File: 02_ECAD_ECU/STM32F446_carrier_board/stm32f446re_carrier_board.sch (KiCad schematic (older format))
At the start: 1 part

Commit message: added submodules in the right place now
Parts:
- gave numbers to parts that had none: 1
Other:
- moved on the sheet: U1
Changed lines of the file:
@@
 $Descr A4 11693 8268
 encoding utf-8
-Sheet 1 1
+Sheet 1 2
 Title ""
 Date ""
@@
 $EndDescr
 $Comp
-L MCU_ST_STM32F4:STM32F446RETx U?
+L MCU_ST_STM32F4:STM32F446RETx U1
 U 1 1 6138BFE8
-P 4000 3800
-F 0 "U?" H 4000 1911 50  0000 C CNN
-F 1 "STM32F446RETx" H 4000 1820 50  0000 C CNN
-F 2 "Package_QFP:LQFP-64_10x10mm_P0.5mm" H 3400 2100 50  0001 R CNN
-F 3 "http://www.st.com/st-web-ui/static/active/en/resource/technical/document/datasheet/DM00141306.pdf" H 4000 3800 50  0001 C CNN
-	1    4000 3800
+P 6700 3750
+F 0 "U1" H 6700 1861 50  0000 C CNN
+F 1 "STM32F446RETx" H 6700 1770 50  0000 C CNN
+F 2 "Package_QFP:LQFP-64_10x10mm_P0.5mm" H 6100 2050 50  0001 R CNN
+F 3 "http://www.st.com/st-web-ui/static/active/en/resource/technical/document/datasheet/DM00141306.pdf" H 6700 3750 50  0001 C CNN
+	1    6700 3750
 	1    0    0    -1
 $EndComp
+$Sheet
+S 9300 3500 1600 1550
+U 614A3ED5
+F0 "connectors" 50
+F1 "connectors.sch" 50
+$EndSheet
 $EndSCHEMATC

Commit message: carrierboard stm32f446 finished v0.1
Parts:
- added C1, C4: 4.7u, Capacitor_SMD:C_1206_3216Metric, symbol Device:C_Small
- added C10, C12: 12p, Capacitor_SMD:C_0603_1608Metric, symbol Device:C_Small
- added C18, C19: 10p, Capacitor_SMD:C_0402_1005Metric, symbol Device:C_Small
- added C2, C3, C5, C6, C7, C?: 100n, Capacitor_SMD:C_0603_1608Metric, symbol Device:C_Small
- added C8: 1u, Capacitor_SMD:C_0805_2012Metric, symbol Device:C_Small
- added C9: 10n, Capacitor_SMD:C_0805_2012Metric, symbol Device:C_Small
- added D1: BLUE, LED_SMD:LED_0603_1608Metric, symbol Device:LED_Small
- added FB2: 600 @ 600MHz, Inductor_SMD:L_0805_2012Metric, symbol Device:Ferrite_Bead_Small
- added H1, H2, H3, H4: MountingHole_Pad, MountingHole:MountingHole_2.2mm_M2_Pad_Via, symbol Mechanical:MountingHole_Pad
- added R1, R4, R? (x2): 10k, Resistor_SMD:R_1206_3216Metric, symbol Device:R_Small
- added R2: 1.5k, Resistor_SMD:R_0805_2012Metric, symbol Device:R_Small
- added R3: 47, Resistor_SMD:R_0603_1608Metric, symbol Device:R_Small
- added R5, R6: 2.2k, Resistor_SMD:R_0805_2012Metric, symbol Device:R_Small
- added SW1: SW_SPDT, max_KiCAD_lib:SPDT_Slide_Switches, symbol Switch:SW_SPDT
- added U3: W25N01GVZEIG_TR, max_KiCAD_lib:SON127P800X600X80-9N, symbol max_KiCAD_lib:W25N01GVZEIG_TR
- added Y1: 16MHz, Crystal:Crystal_SMD_3225-4Pin_3.2x2.5mm, symbol Device:Crystal_GND24_Small
- added Y2: 32.768kHz, Crystal:Crystal_SMD_2012-2Pin_2.0x1.2mm, symbol Device:Crystal_Small
- U1: LCSC part # (none) -> -
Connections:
- net +3V3: now reaches U1.1 (VBAT)
- net +3V3: now also U1.19 (VDD), U1.32 (VDD), U1.48 (VDD), U1.64 (VDD), C1.1, C2.1, C3.1, C5.1, C6.1, C7.1, C?.1, FB2.2, R?.2, R?.2, SW1.1 (A), U3.8 (VCC)
- net PC2: now reaches U1.10 (PC2)
- net PC3: now reaches U1.11 (PC3)
- net GND: now reaches U1.12 (VSSA)
- net GND: now also U1.18 (VSS), U1.31 (VSS), U1.47 (VSS), U1.63 (VSS), C1.2, C10.2, C12.2, C18.2, C19.2, C2.2, C3.2, C4.2, C5.2, C6.2, C7.2, C8.2, C9.2, C?.2, H1.1, H2.1, H3.1, H4.1, R2.2, R4.2, R5.2, R6.2, SW1.3 (C), U3.4 (GND), Y1.2, Y1.4
- net +3.3VA: now reaches U1.13 (VDDA)
- net +3.3VA: now also C8.1, C9.1, FB2.1
- net PA0: now reaches U1.14 (PA0)
- net PA1: now reaches U1.15 (PA1)
- net LED_STATUS: now reaches U1.16 (PA2)
- net LED_STATUS: now also D1.2 (A)
- net PA3: now reaches U1.17 (PA3)
- net PC13: now reaches U1.2 (PC13)
- net PA4: now reaches U1.20 (PA4)
- net PA5: now reaches U1.21 (PA5)
- net PA6: now reaches U1.22 (PA6)
- net PA7: now reaches U1.23 (PA7)
- net PC4: now reaches U1.24 (PC4)
- net PC5: now reaches U1.25 (PC5)
- net PB0: now reaches U1.26 (PB0)
- net PB1: now reaches U1.27 (PB1)
- net at U1.28 (PB2): now also R4.1
- net PB10: now reaches U1.29 (PB10)
- net OSC32_IN: now reaches U1.3 (PC14)
- net OSC32_IN: now also C18.1, Y2.1
- net at U1.30 (VCAP_1): now also C4.1
- net SPI2_!CS: now reaches U1.33 (PB12)
- net SPI2_!CS: now also U3.1 (/CS)
- net SPI2_SCK: now reaches U1.34 (PB13)
- net SPI2_SCK: now also U3.6 (CLK)
- net SPI2_MISO: now reaches U1.35 (PB14)
- net SPI2_MISO: now also U3.2 (DO(IO1))
- net SPI2_MOSI: now reaches U1.36 (PB15)
- net SPI2_MOSI: now also U3.5 (DI(IO0))
- net FLASH_!HOLD: now reaches U1.37 (PC6)
- net FLASH_!HOLD: now also R?.1, U3.7 (/HOLD(IO3))
- net FLASH_!WP: now reaches U1.38 (PC7)
- net FLASH_!WP: now also R?.1, U3.3 (/WP(IO2))
- net PC8: now reaches U1.39 (PC8)
- net OSC32_OUT: now reaches U1.4 (PC15)
- net OSC32_OUT: now also C19.1, Y2.2
- net PC9: now reaches U1.40 (PC9)
- net PA8: now reaches U1.41 (PA8)
- net PA9: now reaches U1.42 (PA9)
- net PA10: now reaches U1.43 (PA10)
- net USB_D-: now reaches U1.44 (PA11)
- net USB_D+: now reaches U1.45 (PA12)
- net SWDIO: now reaches U1.46 (PA13)
- net SWCLK: now reaches U1.49 (PA14)
- net HSE_IN: now reaches U1.5 (PH0)
- net HSE_IN: now also C10.1, Y1.1
- net PA15: now reaches U1.50 (PA15)
- net PC10: now reaches U1.51 (PC10)
- net PC11: now reaches U1.52 (PC11)
- net PC12: now reaches U1.53 (PC12)
- net PD2: now reaches U1.54 (PD2)
- net SWO: now reaches U1.55 (PB3)
- net PB4: now reaches U1.56 (PB4)
- net PB5: now reaches U1.57 (PB5)
- net PB6: now reaches U1.58 (PB6)
- net PB7: now reaches U1.59 (PB7)
- net HSE_OUT: now reaches U1.6 (PH1)
- net HSE_OUT: now also R3.1
- net BOOT0: now reaches U1.60 (BOOT0)
- net BOOT0: now also R1.2
- net I2C1_SCL: now reaches U1.61 (PB8)
- net I2C1_SCL: now also R5.1
- net I2C1_SDA: now reaches U1.62 (PB9)
- net I2C1_SDA: now also R6.1
- net NRST: now reaches U1.7 (NRST)
- net PC0: now reaches U1.8 (PC0)
- net PC1: now reaches U1.9 (PC1)
- new net: R1.1, SW1.2 (B)
- new net: D1.1 (K), R2.1
- new net: C12.1, R3.2, Y1.3
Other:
- note added: "C_load = 2 * (CL -Cstray)\n"
- note added: "ESR 1 Ω \nor below"
- moved on the sheet: U1

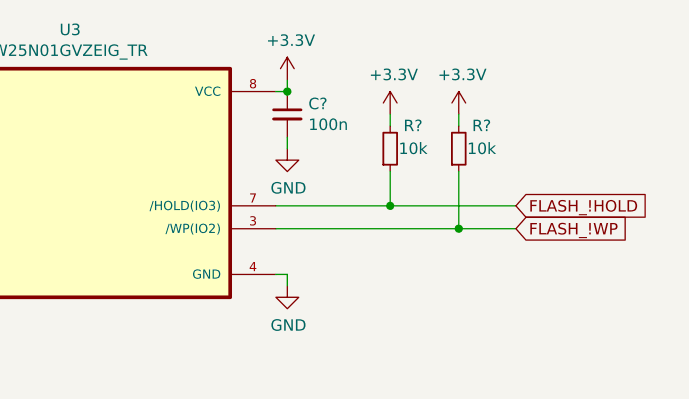
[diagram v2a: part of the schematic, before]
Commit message: created kicad breakoutboard project
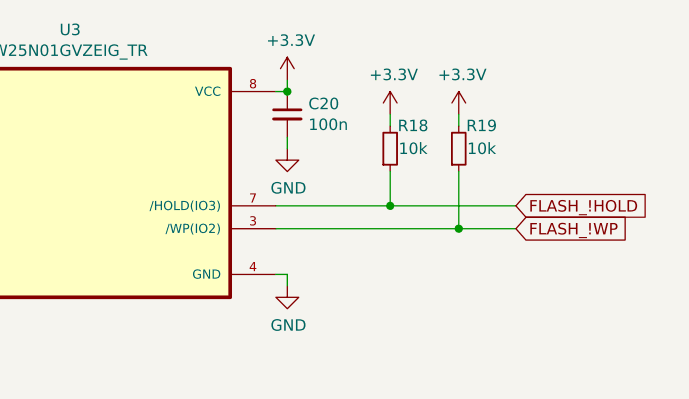
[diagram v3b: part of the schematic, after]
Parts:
- gave numbers to parts that had none: 3
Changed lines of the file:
@@
 	7450 1550 7550 1550
 $Comp
-L power:GND #PWR?
+L power:GND #PWR0138
 U 1 1 614C487E
 P 9400 1900
-F 0 "#PWR?" H 9400 1650 50  0001 C CNN
+F 0 "#PWR0138" H 9400 1650 50  0001 C CNN
 F 1 "GND" H 9405 1727 50  0000 C CNN
 F 2 "" H 9400 1900 50  0001 C CNN
@@
 	9400 1850 9400 1900
 $Comp
-L power:+3.3V #PWR?
+L power:+3.3V #PWR0139
 U 1 1 614CDE88
 P 9400 1000
-F 0 "#PWR?" H 9400 850 50  0001 C CNN
+F 0 "#PWR0139" H 9400 850 50  0001 C CNN
 F 1 "+3.3V" H 9415 1173 50  0000 C CNN
 F 2 "" H 9400 1000 50  0001 C CNN
@@
 	9400 1050 9400 1000
 $Comp
-L Device:C_Small C?
+L Device:C_Small C20
 U 1 1 614D74C0
 P 9400 1150
-F 0 "C?" H 9492 1196 50  0000 L CNN
+F 0 "C20" H 9492 1196 50  0000 L CNN
 F 1 "100n" H 9492 1105 50  0000 L CNN
 F 2 "Capacitor_SMD:C_0603_1608Metric" H 9400 1150 50  0001 C CNN
@@
 Connection ~ 9400 1050
 $Comp
-L power:GND #PWR?
+L power:GND #PWR0140
 U 1 1 614D7DB2
 P 9400 1300
-F 0 "#PWR?" H 9400 1050 50  0001 C CNN
+F 0 "#PWR0140" H 9400 1050 50  0001 C CNN
 F 1 "GND" H 9405 1127 50  0000 C CNN
 F 2 "" H 9400 1300 50  0001 C CNN
@@
 	10400 1650 10150 1650
 $Comp
-L power:+3.3V #PWR?
+L power:+3.3V #PWR0141
 U 1 1 61530514
 P 9850 1150
-F 0 "#PWR?" H 9850 1000 50  0001 C CNN
+F 0 "#PWR0141" H 9850 1000 50  0001 C CNN
 F 1 "+3.3V" H 9865 1323 50  0000 C CNN
 F 2 "" H 9850 1150 50  0001 C CNN
@@
 $EndComp
 $Comp
-L power:+3.3V #PWR?
+L power:+3.3V #PWR0142
 U 1 1 615309F9
 P 10150 1150
-F 0 "#PWR?" H 10150 1000 50  0001 C CNN
+F 0 "#PWR0142" H 10150 1000 50  0001 C CNN
 F 1 "+3.3V" H 10165 1323 50  0000 C CNN
 F 2 "" H 10150 1150 50  0001 C CNN
@@
 $EndComp
 $Comp
-L Device:R_Small R?
+L Device:R_Small R18
 U 1 1 61530C68
 P 9850 1300
-F 0 "R?" H 9950 1200 50  0000 C CNN
+F 0 "R18" H 9950 1200 50  0000 C CNN
 F 1 "10k" H 9950 1300 50  0000 C CNN
 F 2 "Resistor_SMD:R_1206_3216Metric" H 9850 1300 50  0001 C CNN
@@
 	9850 1550 10400 1550
 $Comp
-L Device:R_Small R?
+L Device:R_Small R19
 U 1 1 6154C7CE
 P 10150 1300
-F 0 "R?" H 10250 1200 50  0000 C CNN
+F 0 "R19" H 10250 1200 50  0000 C CNN
 F 1 "10k" H 10250 1300 50  0000 C CNN
 F 2 "Resistor_SMD:R_1206_3216Metric" H 10150 1300 50  0001 C CNN
